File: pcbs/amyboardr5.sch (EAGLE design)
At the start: 150 parts, among them J1 52601-G10-8LF, Q2 S8050, Q5 S8050, U1 PCM9211PT, U15 H11L1SR2M, U16 SPX3819, U2 ESP32­S2­SOLO, U3 SPX3819, U4 TL074CD, U6 HX3608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

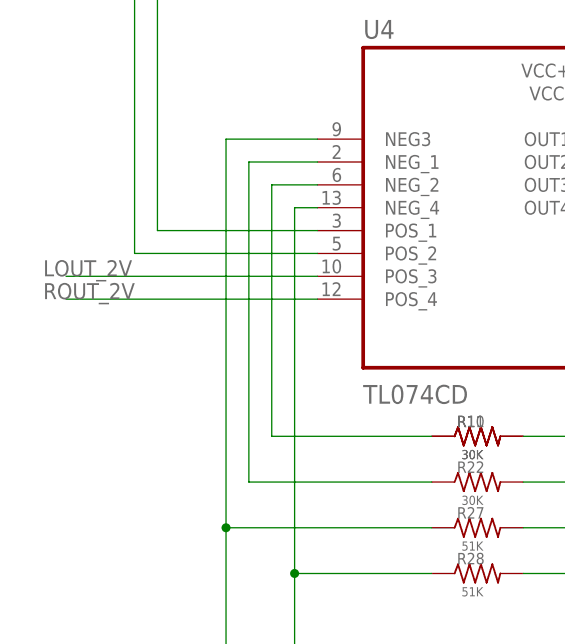
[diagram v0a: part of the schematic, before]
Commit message: CVOUT fixes
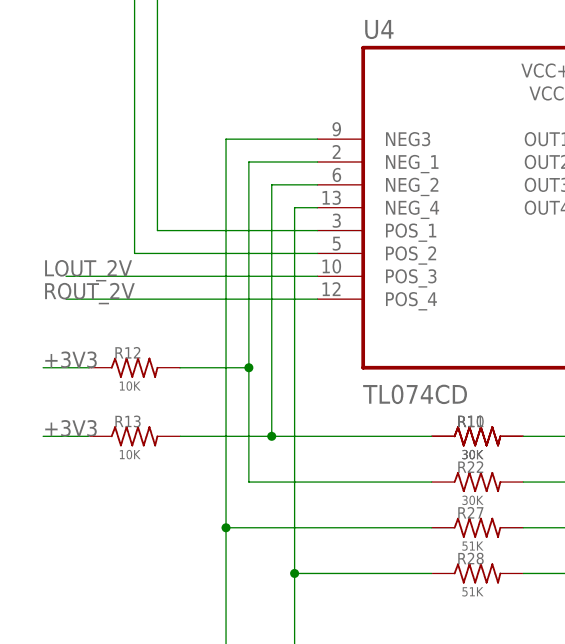
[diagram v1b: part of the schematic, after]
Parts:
- added R12, R13: 10K, adafruit:R-US_R0805
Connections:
- net +3V3: now also R12.1, R13.1
- net N$31: now also R13.2
- net N$33: now also R12.2
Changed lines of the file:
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@@
 <part name="GND10" library="supply1" deviceset="GND" device=""/>
 <part name="C35" library="Discrete" deviceset="C*" device="-0603" value="NC"/>
+<part name="R12" library="adafruit" deviceset="R-US_" device="R0805" value="10K"/>
+<part name="R13" library="adafruit" deviceset="R-US_" device="R0805" value="10K"/>
 </parts>
 <sheets>
@@
 <attribute name="VALUE" x="185.928" y="-22.86" size="1.016" layer="96"/>
 </instance>
+<instance part="R12" gate="G$1" x="-248.92" y="-48.26" smashed="yes">
+<attribute name="NAME" x="-251.206" y="-47.244" size="1.27" layer="95" font="vector"/>
+<attribute name="VALUE" x="-250.698" y="-50.8" size="1.016" layer="96" font="vector" ratio="15"/>
+</instance>
+<instance part="R13" gate="G$1" x="-248.92" y="-55.88" smashed="yes">
+<attribute name="NAME" x="-251.206" y="-54.864" size="1.27" layer="95" font="vector"/>
+<attribute name="VALUE" x="-250.698" y="-58.42" size="1.016" layer="96" font="vector" ratio="15"/>
+</instance>
 </instances>
 <busses>
@@
 <wire x1="196.85" y1="24.13" x2="189.23" y2="24.13" width="0.1524" layer="91"/>
 </segment>
+<segment>
+<pinref part="R12" gate="G$1" pin="1"/>
+<wire x1="-254" y1="-48.26" x2="-259.08" y2="-48.26" width="0.1524" layer="91"/>
+<label x="-259.08" y="-48.26" size="1.778" layer="95"/>
+</segment>
+<segment>
+<pinref part="R13" gate="G$1" pin="1"/>
+<wire x1="-254" y1="-55.88" x2="-259.08" y2="-55.88" width="0.1524" layer="91"/>
+<label x="-259.08" y="-55.88" size="1.778" layer="95"/>
+</segment>
 </net>
 <net name="RESET" class="0">
@@
 <pinref part="U4" gate="A" pin="NEG_2"/>
 <wire x1="-233.68" y1="-27.94" x2="-228.6" y2="-27.94" width="0.1524" layer="91"/>
+<pinref part="R13" gate="G$1" pin="2"/>
+<wire x1="-233.68" y1="-55.88" x2="-243.84" y2="-55.88" width="0.1524" layer="91"/>
+<junction x="-233.68" y="-55.88"/>
 </segment>
 </net>
@@
 <pinref part="R22" gate="G$1" pin="1"/>
 <wire x1="-215.9" y1="-60.96" x2="-236.22" y2="-60.96" width="0.1524" layer="91"/>
-<wire x1="-236.22" y1="-60.96" x2="-236.22" y2="-25.4" width="0.1524" layer="91"/>
+<wire x1="-236.22" y1="-60.96" x2="-236.22" y2="-48.26" width="0.1524" layer="91"/>
 <pinref part="U4" gate="A" pin="NEG_1"/>
+<wire x1="-236.22" y1="-48.26" x2="-236.22" y2="-25.4" width="0.1524" layer="91"/>
 <wire x1="-236.22" y1="-25.4" x2="-228.6" y2="-25.4" width="0.1524" layer="91"/>
-</segment>
-</net>
+<pinref part="R12" gate="G$1" pin="2"/>
+<wire x1="-236.22" y1="-48.26" x2="-243.84" y2="-48.26" width="0.1524" layer="91"/>
+<junction x="-236.22" y="-48.26"/>
+</segment>
+</net>

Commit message: dans fixes
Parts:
- R5: value 10K -> 30K
- R6: value 15K -> 10K
- R8: value 30K -> 15K
- renumbered J1 to MODULAR_PSU
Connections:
- removed net N$17 (its old number): CV_IN1.TIP, R8.1
- new net N$16: C9.1, R21.2
- new net N$19: CV_IN1.TIP, R5.1
- new net N$23: C10.1, R8.2
- net +3V3: now also R6.1; no longer R5.1
- net 12V: now also C32.1, U3.EN, U3.VIN
- net ADC1: now also R6.2, R8.1; no longer C10.1, R6.1, R8.2
- net ADC2: no longer C9.1
- net GND: now also CV_IN2.EARTH, U1.RXIN1; no longer R21.2, R6.2
- net VPWR: no longer C32.1, U3.EN, U3.VIN
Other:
- note added: "MIDI"
- note added: "PCM5101 DAC"
- note added: "PCM9211 ADC and SPDIF"
- note removed: "DAC and ADC and MIDI"
- note removed: "PCM9211"
- moved on the sheet: 1-10VPP, C10, C103, C2, C21, C22, C23, C24, C26, C3, C9, CV_IN1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

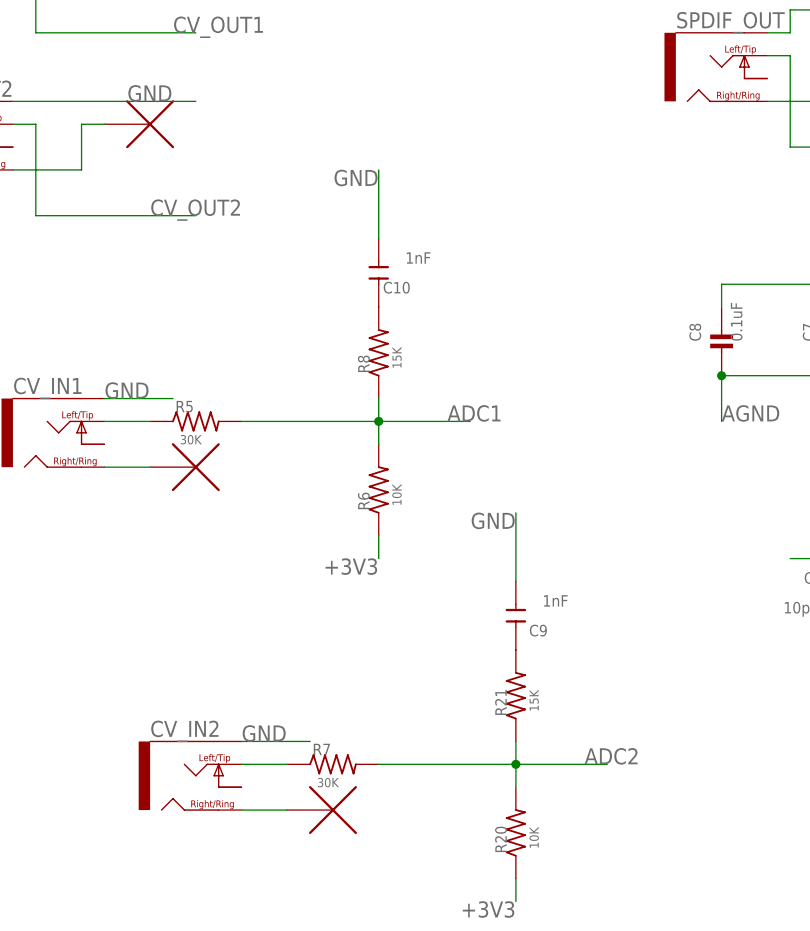
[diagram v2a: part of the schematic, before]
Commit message: ADC cap in parallel
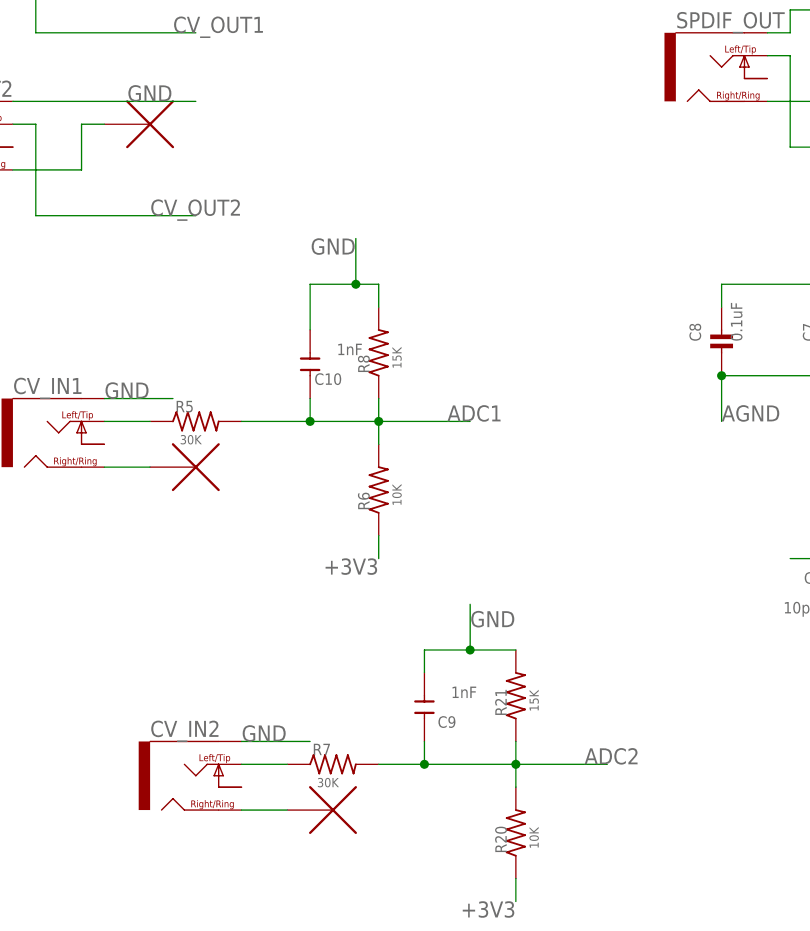
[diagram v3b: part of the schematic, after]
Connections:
- removed net N$16: C9.1, R21.2
- removed net N$23: C10.1, R8.2
- net ADC1: now also C10.1
- net ADC2: now also C9.1
- net GND: now also R21.2, R8.2
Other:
- moved on the sheet: C10, C9
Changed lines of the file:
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@@
 <attribute name="VALUE" x="-52.578" y="-60.96" size="1.016" layer="96" font="vector" ratio="15"/>
 </instance>
-<instance part="C9" gate="C" x="-30.48" y="-41.91" smashed="yes" rot="R90">
-<attribute name="NAME" x="-26.924" y="-42.926" size="1.27" layer="95" ratio="10" rot="R180"/>
-<attribute name="VALUE" x="-24.638" y="-39.624" size="1.27" layer="96" ratio="10" rot="R180"/>
+<instance part="C9" gate="C" x="-40.64" y="-52.07" smashed="yes" rot="R90">
+<attribute name="NAME" x="-37.084" y="-53.086" size="1.27" layer="95" ratio="10" rot="R180"/>
+<attribute name="VALUE" x="-34.798" y="-49.784" size="1.27" layer="96" ratio="10" rot="R180"/>
 </instance>
 <instance part="MODULAR_PSU" gate="G$1" x="289.56" y="91.44" smashed="yes">
@@
 <attribute name="VALUE" x="-67.818" y="-22.86" size="1.016" layer="96" font="vector" ratio="15"/>
 </instance>
-<instance part="C10" gate="C" x="-45.72" y="-3.81" smashed="yes" rot="R90">
-<attribute name="NAME" x="-42.164" y="-4.826" size="1.27" layer="95" ratio="10" rot="R180"/>
-<attribute name="VALUE" x="-39.878" y="-1.524" size="1.27" layer="96" ratio="10" rot="R180"/>
+<instance part="C10" gate="C" x="-53.34" y="-13.97" smashed="yes" rot="R90">
+<attribute name="NAME" x="-49.784" y="-14.986" size="1.27" layer="95" ratio="10" rot="R180"/>
+<attribute name="VALUE" x="-47.498" y="-11.684" size="1.27" layer="96" ratio="10" rot="R180"/>
 </instance>
 <instance part="CV_IN1" gate="G$1" x="-81.28" y="-22.86" smashed="yes">
@@
 </segment>
 <segment>
-<pinref part="C9" gate="C" pin="2"/>
-<wire x1="-30.48" y1="-38.1" x2="-30.48" y2="-30.48" width="0.1524" layer="91"/>
-<label x="-30.48" y="-30.48" size="1.778" layer="95" rot="R180"/>
-</segment>
-<segment>
 <pinref part="MODULAR_PSU" gate="G$1" pin="03"/>
 <wire x1="276.86" y1="93.98" x2="269.24" y2="93.98" width="0.1524" layer="91"/>
@@
 <segment>
 <pinref part="C10" gate="C" pin="2"/>
-<wire x1="-45.72" y1="0" x2="-45.72" y2="7.62" width="0.1524" layer="91"/>
-<label x="-45.72" y="7.62" size="1.778" layer="95" rot="R180"/>
+<wire x1="-53.34" y1="-10.16" x2="-53.34" y2="-5.08" width="0.1524" layer="91"/>
+<label x="-48.26" y="0" size="1.778" layer="95" rot="R180"/>
+<pinref part="R8" gate="G$1" pin="2"/>
+<wire x1="-45.72" y1="-7.62" x2="-45.72" y2="-5.08" width="0.1524" layer="91"/>
+<wire x1="-45.72" y1="-5.08" x2="-48.26" y2="-5.08" width="0.1524" layer="91"/>
+<wire x1="-48.26" y1="-5.08" x2="-53.34" y2="-5.08" width="0.1524" layer="91"/>
+<wire x1="-48.26" y1="-5.08" x2="-48.26" y2="0" width="0.1524" layer="91"/>
+<junction x="-48.26" y="-5.08"/>
+</segment>
+<segment>
+<pinref part="C9" gate="C" pin="2"/>
+<wire x1="-40.64" y1="-48.26" x2="-40.64" y2="-45.72" width="0.1524" layer="91"/>
+<pinref part="R21" gate="G$1" pin="2"/>
+<wire x1="-40.64" y1="-45.72" x2="-35.56" y2="-45.72" width="0.1524" layer="91"/>
+<wire x1="-35.56" y1="-45.72" x2="-30.48" y2="-45.72" width="0.1524" layer="91"/>
+<wire x1="-35.56" y1="-45.72" x2="-35.56" y2="-40.64" width="0.1524" layer="91"/>
+<junction x="-35.56" y="-45.72"/>
+<label x="-35.56" y="-43.18" size="1.778" layer="95"/>
 </segment>
 </net>
@@
 <label x="-38.1" y="-20.32" size="1.778" layer="95"/>
 <pinref part="R5" gate="G$1" pin="2"/>
-<wire x1="-60.96" y1="-20.32" x2="-45.72" y2="-20.32" width="0.1524" layer="91"/>
+<wire x1="-60.96" y1="-20.32" x2="-53.34" y2="-20.32" width="0.1524" layer="91"/>
+<pinref part="C10" gate="C" pin="1"/>
+<wire x1="-53.34" y1="-20.32" x2="-45.72" y2="-20.32" width="0.1524" layer="91"/>
+<wire x1="-53.34" y1="-20.32" x2="-53.34" y2="-17.78" width="0.1524" layer="91"/>
+<junction x="-53.34" y="-20.32"/>
 </segment>
 </net>
@@
 <label x="-22.86" y="-58.42" size="1.778" layer="95"/>
 <pinref part="R7" gate="G$1" pin="2"/>
-<wire x1="-45.72" y1="-58.42" x2="-30.48" y2="-58.42" width="0.1524" layer="91"/>
+<wire x1="-45.72" y1="-58.42" x2="-40.64" y2="-58.42" width="0.1524" layer="91"/>
+<pinref part="C9" gate="C" pin="1"/>
+<wire x1="-40.64" y1="-58.42" x2="-30.48" y2="-58.42" width="0.1524" layer="91"/>
+<wire x1="-40.64" y1="-55.88" x2="-40.64" y2="-58.42" width="0.1524" layer="91"/>
+<junction x="-40.64" y="-58.42"/>
 </segment>
 </net>
@@
 </segment>
 </net>
-<net name="N$16" class="0">
-<segment>
-<pinref part="R21" gate="G$1" pin="2"/>
-<pinref part="C9" gate="C" pin="1"/>
-</segment>
-</net>
 <net name="N$17" class="0">
 <segment>
@@
 </segment>
 </net>
-<net name="N$23" class="0">
-<segment>
-<pinref part="R8" gate="G$1" pin="2"/>
-<pinref part="C10" gate="C" pin="1"/>
-</segment>
-</net>
